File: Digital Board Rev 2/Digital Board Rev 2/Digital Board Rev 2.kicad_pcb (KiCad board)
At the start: 4 copper layers, 59.5 x 96.3 mm, 91 parts, among them J1 Conn_01x02_Male, J10 AudioJack3_Switch, J11 Conn_01x10_Female, J12 Barrel_Jack, J13 Conn_01x06_Female, J14 Conn_01x06_Female, J15 Conn_01x03_Male, J2 Conn_01x02_Male, J3 Conn_01x06_Male, J4 Conn_01x08_Female, J5 AudioJack3_Switch, J6 AudioJack3_Switch, J7 AudioJack3_Switch, J8 AudioJack3_Switch, J9 AudioJack3_Switch, K1 IM05, Q1 BSS83P, Q25 MMBT3904, SW1 SW_SPDT_MSM, SW2 SW_SPDT_MSM, SW3 SW_SPDT_MSM, U1 STM32F303R6Tx, U26 TLP222A-2, U27 NCP1117-3.3_SOT223, U28 TC7662Bx0A, Y1 8MHz

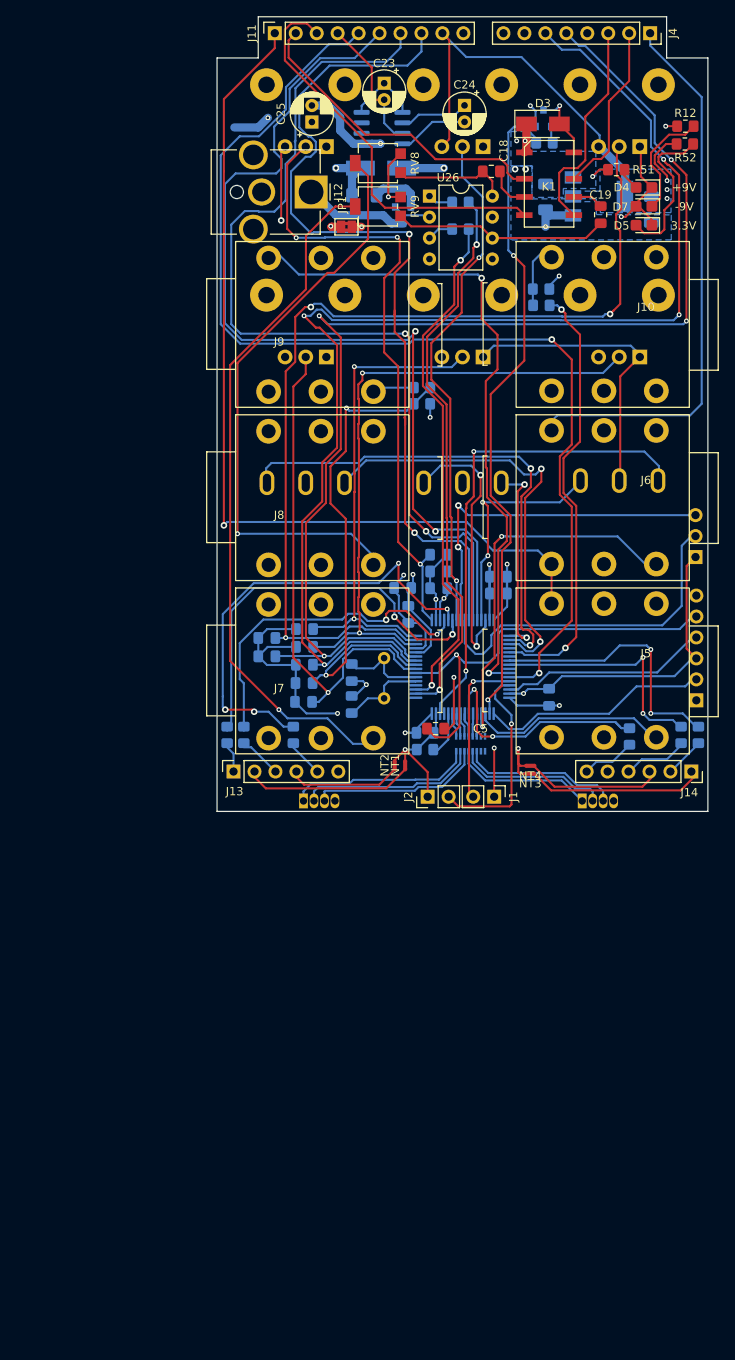
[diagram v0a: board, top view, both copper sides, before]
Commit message: Added projects for V3 boards
Made V3 projects, started with a few changes in both schematics.
Migrated to KiCad 9.0.
Repo needs a bit of reorg
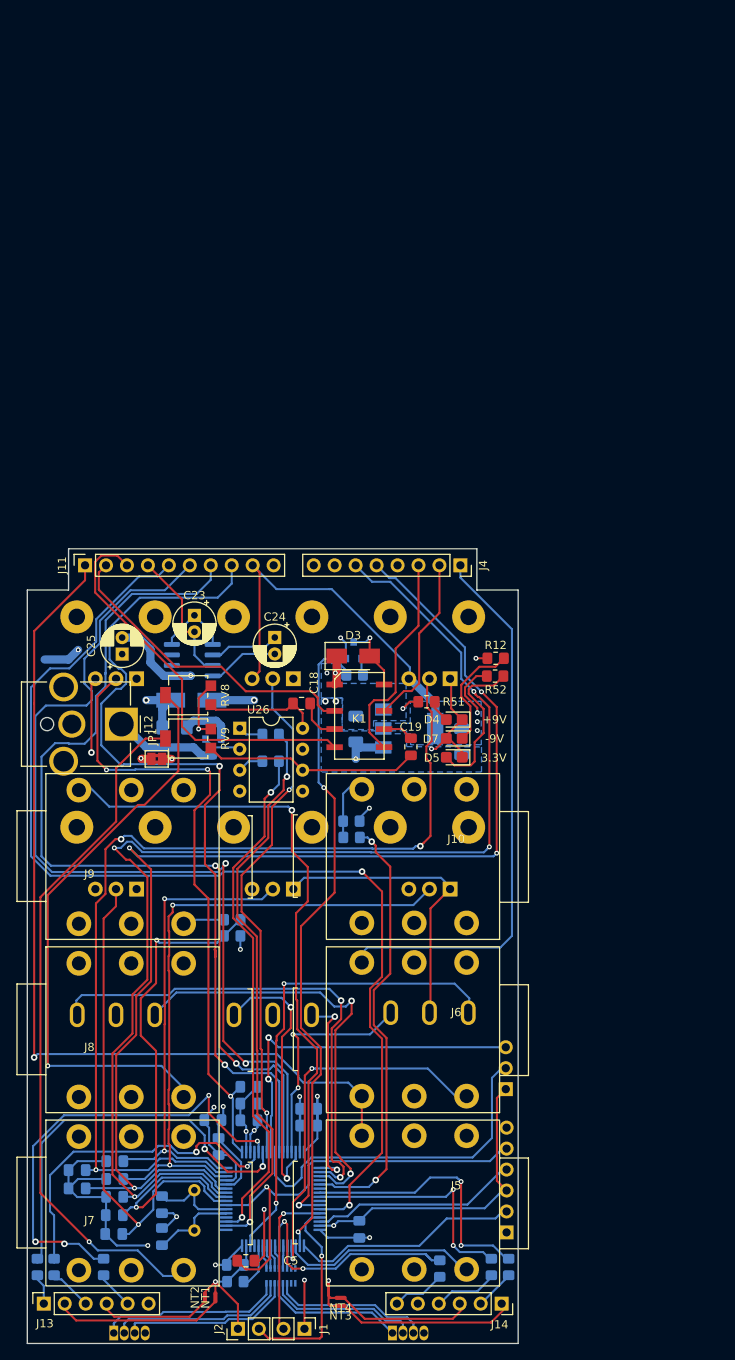
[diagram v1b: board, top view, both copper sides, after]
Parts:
- moved C9 68.5 mm to (123.4, 172.7)
- moved C1 68.5 mm to (134.4, 168.1)
- moved C10 68.5 mm to (122.8, 169.5)
- moved C12 68.5 mm to (106.3, 175.6)
- moved C13 68.5 mm to (110.9, 174.5)
- moved C14 68.5 mm to (127.1, 165.5)
- moved C15 68.5 mm to (110.7, 183.3)
- moved C16 68.5 mm to (110.8, 181.0)
- moved C17 68.5 mm to (110.8, 178.8)
- moved C18 68.5 mm to (133.5, 119.0)
- moved C19 68.5 mm to (146.8, 124.2)
- moved C2 68.5 mm to (116.6, 183.6)
- moved C21 68.5 mm to (140.1, 122.1)
- moved C22 68.5 mm to (152.9, 123.6)
- moved C24 68.5 mm to (130.2, 111.0)
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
